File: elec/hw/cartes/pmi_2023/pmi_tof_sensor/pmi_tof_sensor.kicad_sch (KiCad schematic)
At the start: 31 parts, among them J1 tof_sensor_female, Q1 BSS84, Q4 BSS8402DW-7-F, U3 VL53L1CXV0FY1, U4 VL53L5CXV0GC

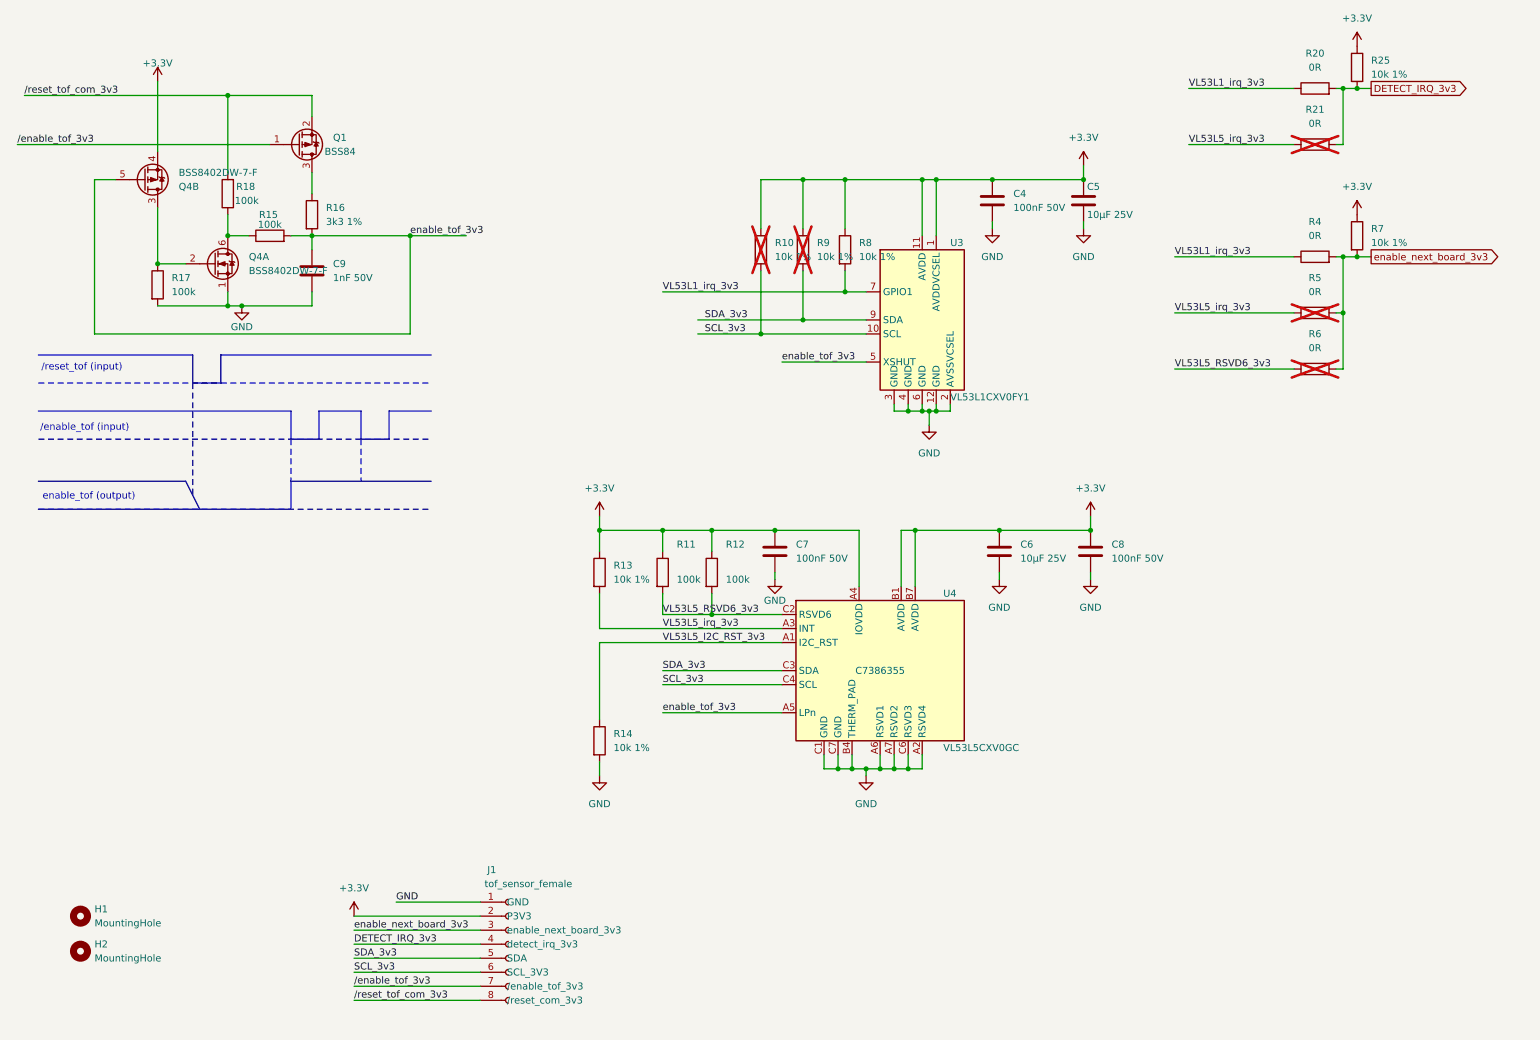
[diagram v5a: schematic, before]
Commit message: bom updated and component selection optimized to decrease bom cost
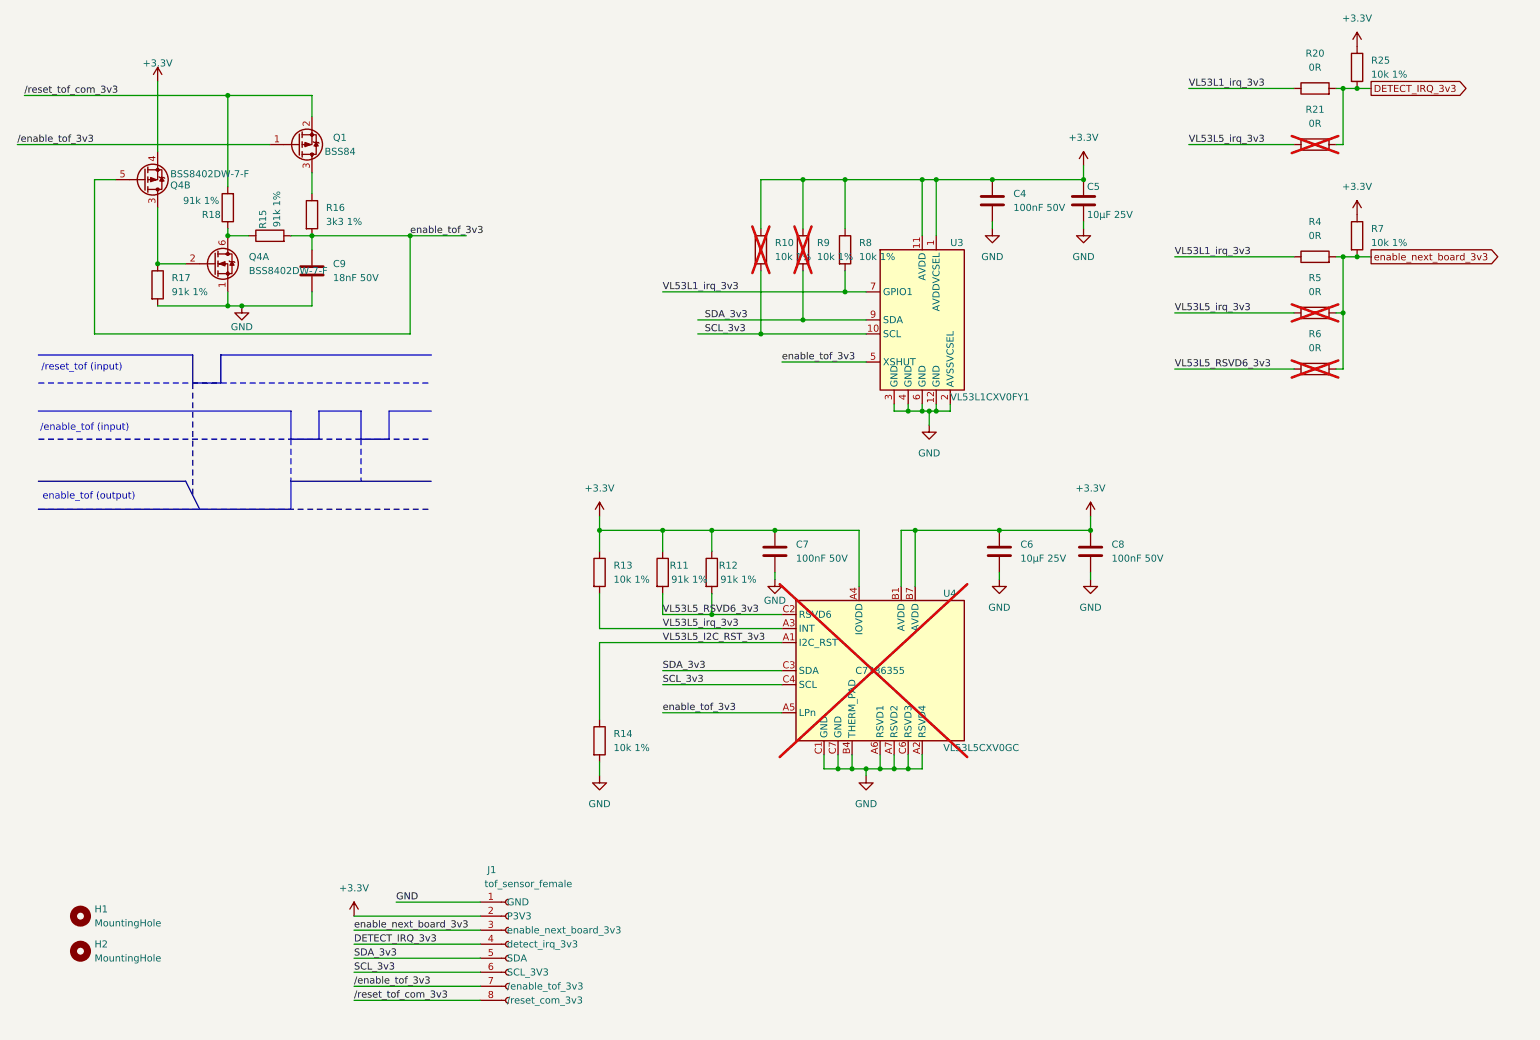
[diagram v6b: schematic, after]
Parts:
- C9: value 1nF 50V -> 18nF 50V; symbol cocotter_capacitors:C_1nF_50V_0603 -> cocotter_capacitors:C_18nF_50V_0603; JLCPCB Part # (none) -> C107079; Specification 1nF 50V X7R 0603 -> 18nF 50V X7R 0603
- R11, R12, R15, R17, R18: value 100k -> 91k 1%; symbol cocotter_resistors:R_100k_0603_1% -> cocotter_resistors:R_91k_0603_1%; JLCPCB C25803 -> (none); JLCPCB Part # (none) -> C23265; Specification 100k 0603 1% 100mW -> 91k 0603 1% 100mW; mouser 603-RC0603FR-10100KL -> (none)
- U4: now not fitted
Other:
- moved on the sheet: R18
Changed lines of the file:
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@@
 	(wire
 		(pts
-			(xy 52.07 50.8) (xy 52.07 54.61)
+			(xy 52.07 53.34) (xy 52.07 54.61)
 		)
 		(stroke
@@
 	(wire
 		(pts
-			(xy 52.07 43.18) (xy 52.07 29.21)
+			(xy 52.07 45.72) (xy 52.07 29.21)
 		)
 		(stroke
@@
 	)
 	(symbol
-		(lib_id "cocotter_capacitors:C_1nF_50V_0603")
+		(lib_id "cocotter_capacitors:C_18nF_50V_0603")
 		(at 67.31 60.96 0)
 		(unit 1)
@@
 			)
 		)
-		(property "Value" "1nF 50V"
+		(property "Value" "18nF 50V"
 			(at 71.12 62.2299 0)
 			(effects
@@
 			)
 		)
-		(property "Specification" "1nF 50V X7R 0603 "
+		(property "Specification" "18nF 50V X7R 0603 "
 			(at 67.31 60.96 0)
 			(effects
@@
 			)
 		)
+		(property "JLCPCB Part #" "C107079 "
+			(at 67.31 60.96 0)
+			(effects
+				(font
+					(size 1.27 1.27)
+				)
+				(hide yes)
+			)
+		)
 		(pin "1"
 		)
@@
 	)
 	(symbol
-		(lib_id "cocotter_resistors:R_100k_0603_1%")
+		(lib_id "cocotter_resistors:R_91k_0603_1%")
 		(at 130.81 115.57 0)
 		(unit 1)
@@
 		(dnp no)
 		(property "Reference" "R11"
-			(at 133.35 110.49 0)
+			(at 132.08 114.3 0)
 			(effects
 				(font
@@
 			)
 		)
-		(property "Value" "100k"
-			(at 133.35 116.84 0)
+		(property "Value" "91k 1%"
+			(at 135.636 116.84 0)
 			(effects
 				(font
 					(size 1.27 1.27)
 				)
-				(justify left)
 			)
 		)
@@
 			)
 		)
-		(property "Specification" "100k 0603 1% 100mW"
+		(property "Specification" "91k 0603 1% 100mW"
 			(at 130.81 115.57 0)
 			(effects
@@
 			)
 		)
-		(property "mouser" "603-RC0603FR-10100KL"
+		(property "mouser" ""
 			(at 130.81 115.57 0)
 			(effects
@@
 			)
 		)
-		(property "JLCPCB" "C25803"
+		(property "JLCPCB Part #" "C23265"
 			(at 130.81 115.57 0)
 			(effects
@@
 	)
 	(symbol
-		(lib_id "cocotter_resistors:R_100k_0603_1%")
-		(at 52.07 46.99 180)
+		(lib_id "cocotter_resistors:R_91k_0603_1%")
+		(at 52.07 49.53 180)
 		(unit 1)
 		(exclude_from_sim no)
@@
 		(dnp no)
 		(property "Reference" "R18"
-			(at 53.594 45.72 0)
+			(at 50.8 50.8 0)
 			(effects
 				(font
 					(size 1.27 1.27)
 				)
-				(justify right)
+				(justify left)
 			)
 		)
-		(property "Value" "100k"
-			(at 53.34 48.26 0)
+		(property "Value" "91k 1%"
+			(at 47.244 48.26 0)
 			(effects
 				(font
 					(size 1.27 1.27)
 				)
-				(justify right)
 			)
 		)
 		(property "Footprint" "cocotter_resistor:r0603_reflow"
-			(at 53.848 46.99 90)
+			(at 53.848 49.53 90)
 			(effects
 				(font
@@
 		)
 		(property "Datasheet" "~"
-			(at 52.07 46.99 0)
+			(at 52.07 49.53 0)
 			(effects
 				(font
@@
 		)
 		(property "Description" "Resistor"
-			(at 52.07 46.99 0)
+			(at 52.07 49.53 0)
 			(effects
 				(font
@@
 			)
 		)
-		(property "Specification" "100k 0603 1% 100mW"
-			(at 52.07 46.99 0)
+		(property "Specification" "91k 0603 1% 100mW"
+			(at 52.07 49.53 0)
 			(effects
 				(font
@@
 			)
 		)
-		(property "mouser" "603-RC0603FR-10100KL"
-			(at 52.07 46.99 0)
+		(property "mouser" ""
+			(at 52.07 49.53 0)
 			(effects
 				(font
@@
 			)
 		)
-		(property "JLCPCB" "C25803"
-			(at 52.07 46.99 0)
+		(property "JLCPCB Part #" "C23265"
+			(at 52.07 49.53 0)
 			(effects
 				(font
@@
 	)
 	(symbol
-		(lib_id "cocotter_resistors:R_100k_0603_1%")
+		(lib_id "cocotter_resistors:R_91k_0603_1%")
 		(at 139.7 115.57 0)
 		(unit 1)
@@
 		(dnp no)
 		(property "Reference" "R12"
-			(at 142.24 110.49 0)
+			(at 140.97 114.3 0)
 			(effects
 				(font
@@
 			)
 		)
-		(property "Value" "100k"
-			(at 142.24 116.84 0)
+		(property "Value" "91k 1%"
+			(at 144.526 116.84 0)
 			(effects
 				(font
 					(size 1.27 1.27)
 				)
-				(justify left)
 			)
 		)
@@
 			)
 		)
-		(property "Specification" "100k 0603 1% 100mW"
+		(property "Specification" "91k 0603 1% 100mW"
 			(at 139.7 115.57 0)
 			(effects
@@
 			)
 		)
-		(property "mouser" "603-RC0603FR-10100KL"
+		(property "mouser" ""
 			(at 139.7 115.57 0)
 			(effects
@@
 			)
 		)
-		(property "JLCPCB" "C25803"
+		(property "JLCPCB Part #" "C23265"
 			(at 139.7 115.57 0)
 			(effects
@@
 	)
 	(symbol
-		(lib_id "cocotter_resistors:R_100k_0603_1%")
+		(lib_id "cocotter_resistors:R_91k_0603_1%")
 		(at 59.69 54.61 90)
 		(unit 1)
@@
 		(dnp no)
 		(property "Reference" "R15"
-			(at 59.436 50.8 90)
+			(at 58.42 53.34 0)
 			(effects
 				(font
 					(size 1.27 1.27)
 				)
+				(justify left)
 			)
 		)
-		(property "Value" "100k"
-			(at 59.69 52.578 90)
+		(property "Value" "91k 1%"
+			(at 60.96 49.784 0)
 			(effects
 				(font
@@
 			)
 		)
-		(property "Specification" "100k 0603 1% 100mW"
+		(property "Specification" "91k 0603 1% 100mW"
 			(at 59.69 54.61 0)
 			(effects
@@
 			)
 		)
-		(property "mouser" "603-RC0603FR-10100KL"
+		(property "mouser" ""
 			(at 59.69 54.61 0)
 			(effects
@@
 			)
 		)
-		(property "JLCPCB" "C25803"
+		(property "JLCPCB Part #" "C23265"
 			(at 59.69 54.61 0)
 			(effects
@@
 		(on_board yes)
 		(dnp no)
-		(fields_autoplaced yes)
 		(property "Reference" "Q4"
-			(at 43.18 45.7201 0)
+			(at 41.656 45.466 0)
 			(effects
 				(font
@@
 		)
 		(property "Value" "BSS8402DW-7-F"
-			(at 43.18 43.1801 0)
+			(at 41.656 43.434 0)
 			(effects
 				(font
@@
 		(in_bom yes)
 		(on_board yes)
-		(dnp no)
+		(dnp yes)
 		(property "Reference" "U4"
 			(at 181.61 119.38 0)
@@
 	)
 	(symbol
-		(lib_id "cocotter_resistors:R_100k_0603_1%")
+		(lib_id "cocotter_resistors:R_91k_0603_1%")
 		(at 39.37 63.5 0)
 		(unit 1)
@@
 			)
 		)
-		(property "Value" "100k"
+		(property "Value" "91k 1%"
 			(at 41.91 64.7699 0)
 			(effects
@@
 			)
 		)
-		(property "Specification" "100k 0603 1% 100mW"
+		(property "Specification" "91k 0603 1% 100mW"
 			(at 39.37 63.5 0)
 			(effects
@@
 			)
 		)
-		(property "mouser" "603-RC0603FR-10100KL"
+		(property "mouser" ""
 			(at 39.37 63.5 0)
 			(effects
@@
 			)
 		)
-		(property "JLCPCB" "C25803"
+		(property "JLCPCB Part #" "C23265"
 			(at 39.37 63.5 0)
 			(effects

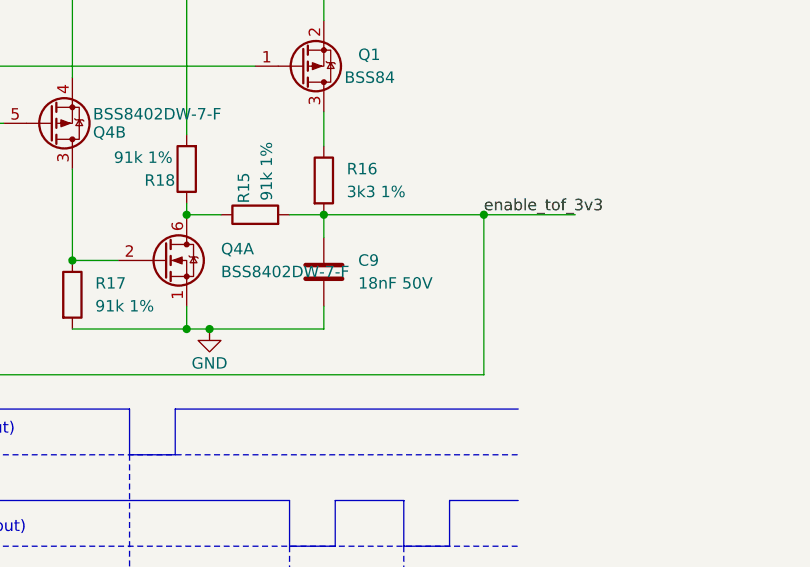
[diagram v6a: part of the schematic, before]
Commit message: 18nF capacitors replaced by 2nF
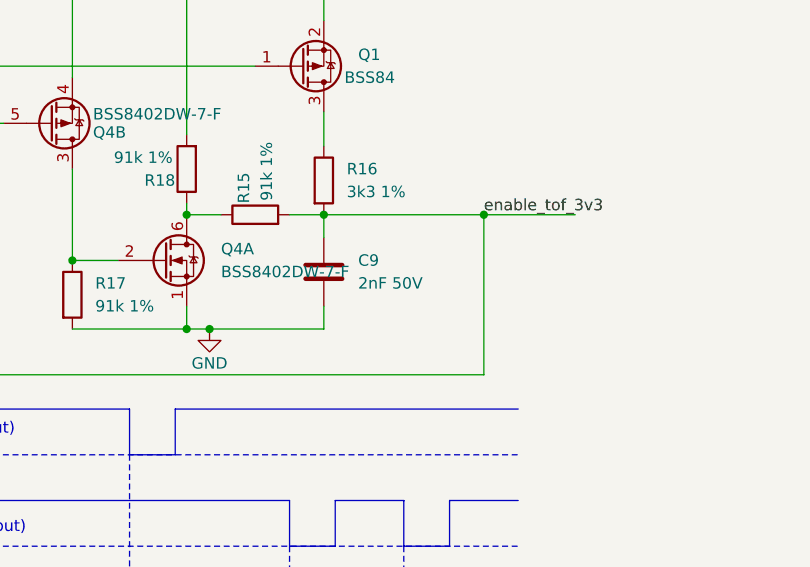
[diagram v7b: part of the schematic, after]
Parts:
- C9: value 18nF 50V -> 2nF 50V; symbol cocotter_capacitors:C_18nF_50V_0603 -> cocotter_capacitors:C_2nF_50V_0603; JLCPCB Part # C107079 -> C282245; Specification 18nF 50V X7R 0603 -> 2nF 50V X7R 0603
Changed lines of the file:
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@@
 	)
 	(symbol
-		(lib_id "cocotter_capacitors:C_18nF_50V_0603")
+		(lib_id "cocotter_capacitors:C_2nF_50V_0603")
 		(at 67.31 60.96 0)
 		(unit 1)
@@
 			)
 		)
-		(property "Value" "18nF 50V"
+		(property "Value" "2nF 50V"
 			(at 71.12 62.2299 0)
 			(effects
@@
 			)
 		)
-		(property "Specification" "18nF 50V X7R 0603 "
+		(property "Specification" "2nF 50V X7R 0603 "
 			(at 67.31 60.96 0)
 			(effects
@@
 			)
 		)
-		(property "JLCPCB Part #" "C107079 "
+		(property "JLCPCB Part #" "C282245"
 			(at 67.31 60.96 0)
 			(effects
